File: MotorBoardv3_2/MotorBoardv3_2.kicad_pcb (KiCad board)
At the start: 2 copper layers, 128.3 x 158.1 mm, 98 parts, among them J1 Bump0, J11 GP2Y0A41SK0F, J12 GP2Y0A41SK0F, J13 GP2Y0A41SK0F, J15 7.2, J16 LP5.0, J17 ELA, J18 ERA, J19 Voltage Display, J2 Bump1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

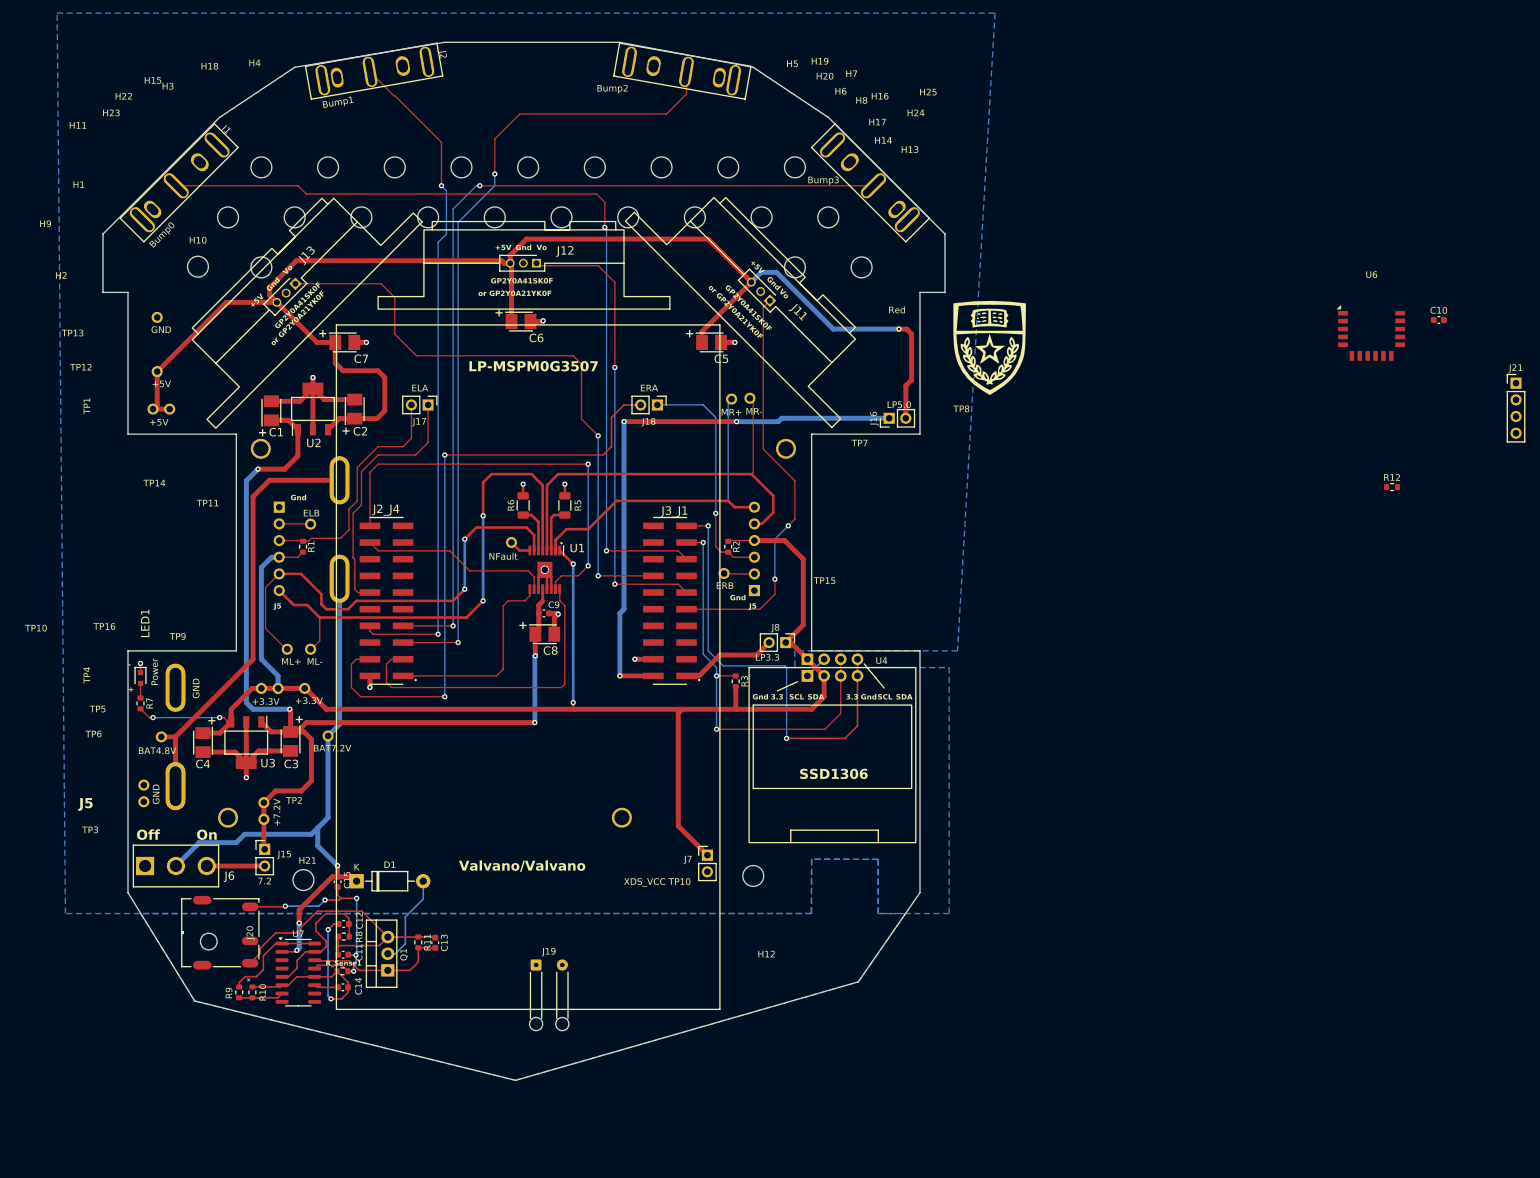
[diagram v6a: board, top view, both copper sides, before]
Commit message: routed RN4871 eval board pins
Also changed the positions of some silkscreen labels
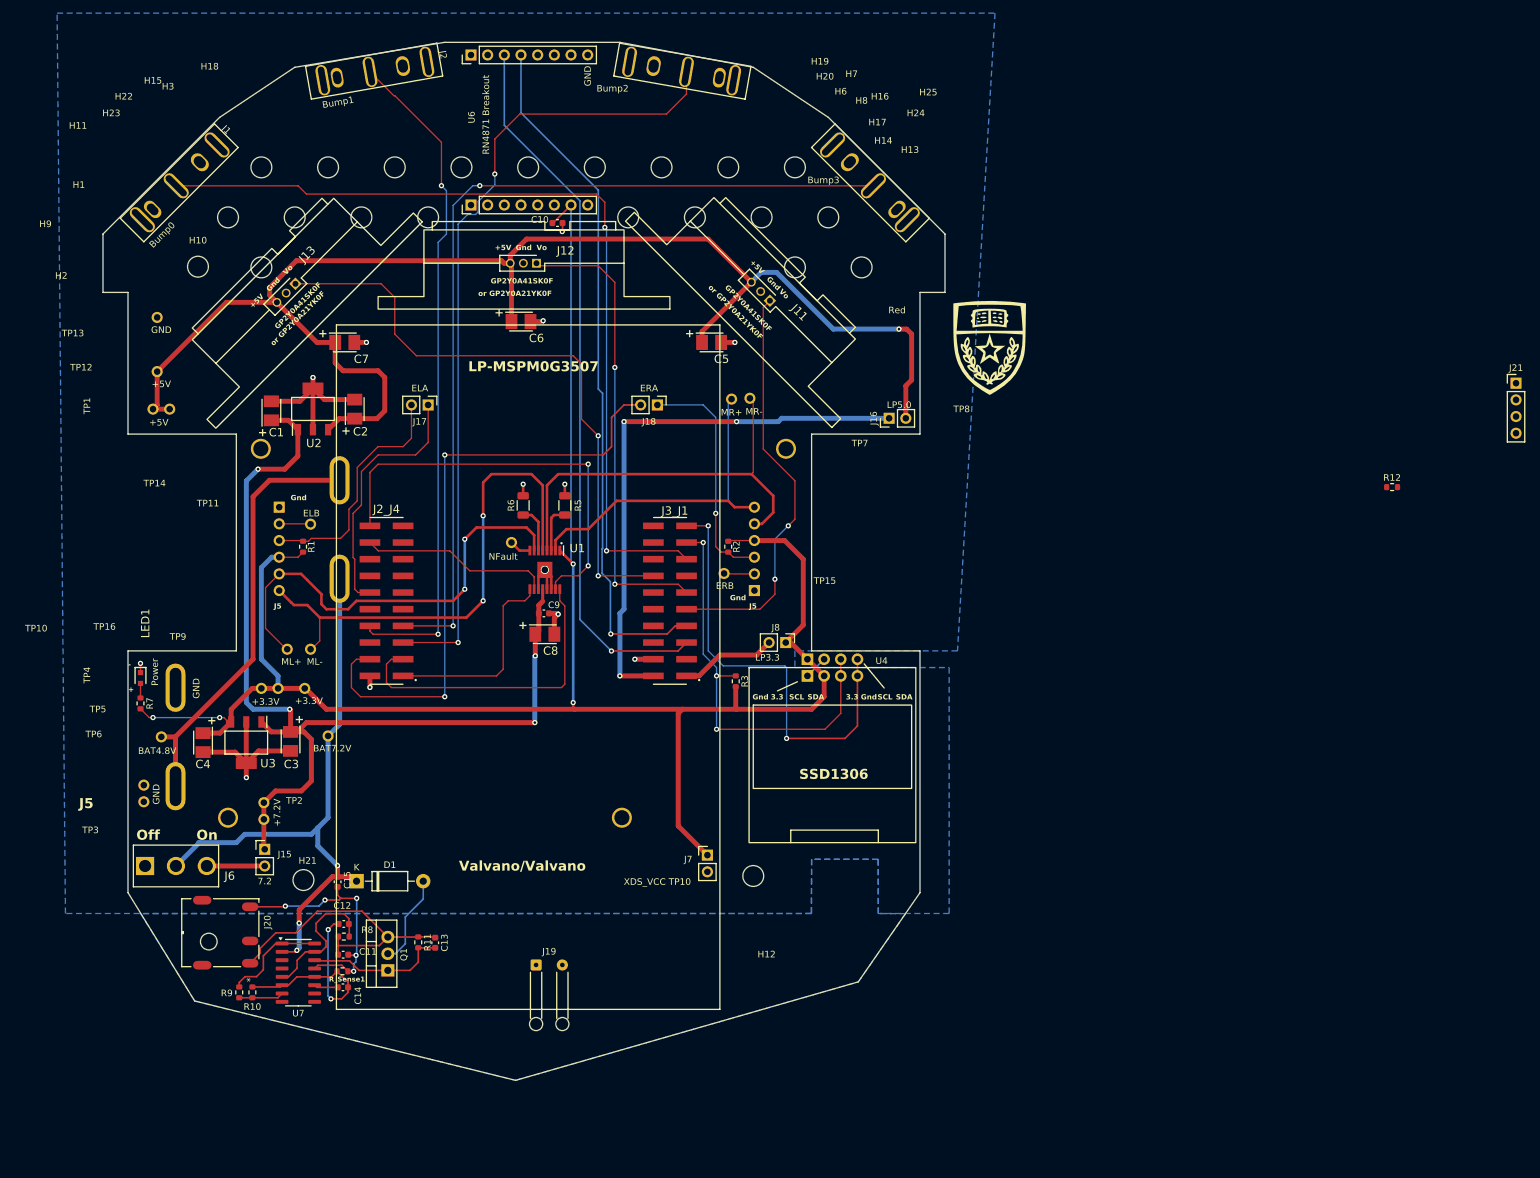
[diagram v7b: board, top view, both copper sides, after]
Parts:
- removed H4, H5: ~, RSLK2:MountingHole_4_40
- U6: footprint RF_Module:Microchip_RN4871 -> VoltageDisplay:RN4871_eval
- moved C10 135.1 mm to (113.7, 51.7)
- moved U6 119.0 mm to (120.1, 50.9), turned to 90 degrees
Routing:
- net PA9: track 0.00 -> 110.8 mm, vias 0 -> 1
- net PA8: track 0.00 -> 106.0 mm, vias 0 -> 1
- net +3V3: track 233.3 -> 292.1 mm
- net GND: track 113.5 -> 114.9 mm, vias 14 -> 15
- net PA28: track 122.8 -> 123.5 mm
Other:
- board text added: "RN4871 Breakout"

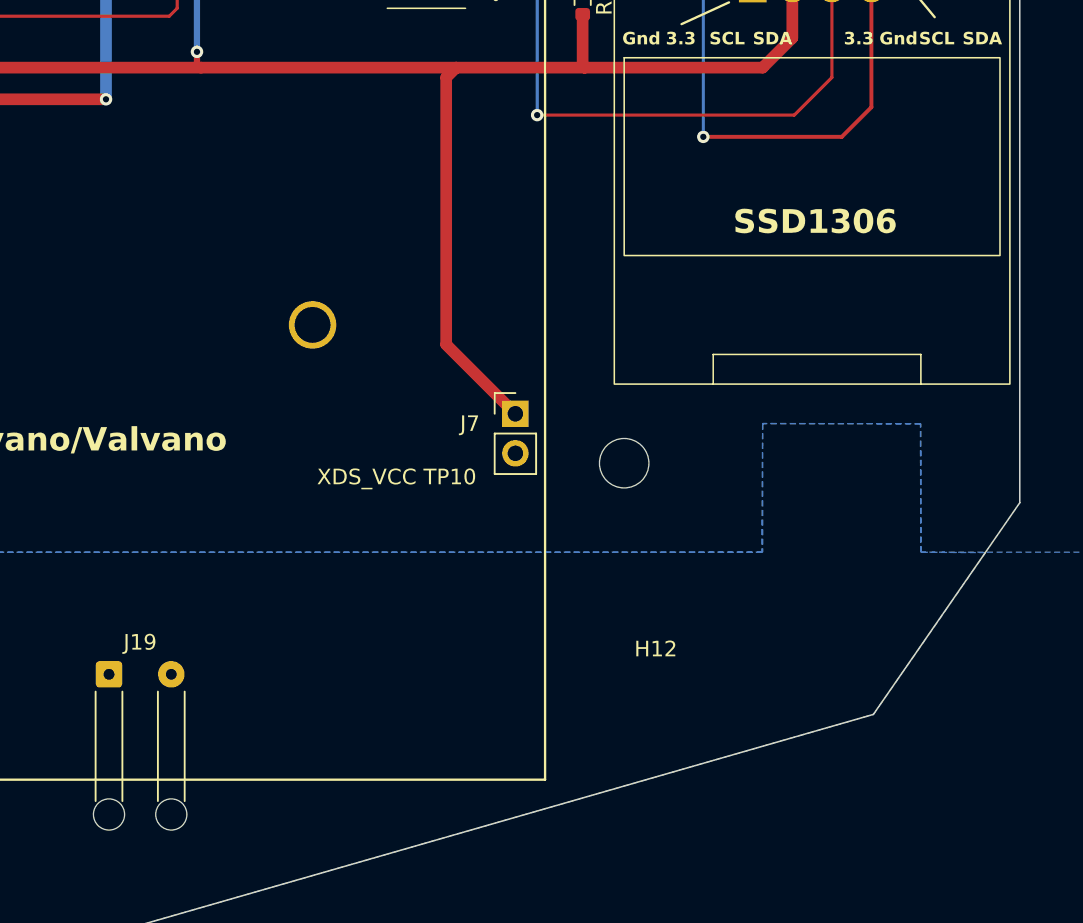
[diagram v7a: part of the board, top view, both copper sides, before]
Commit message: Added voltage display
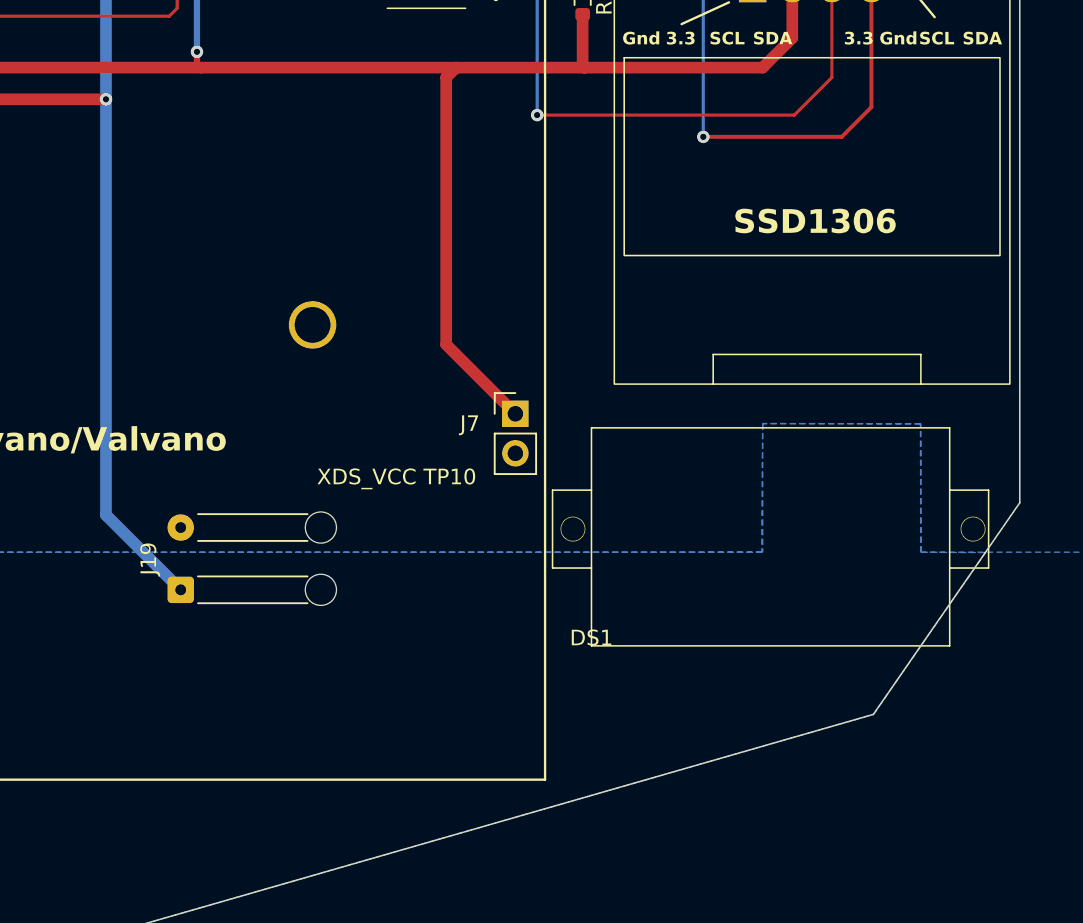
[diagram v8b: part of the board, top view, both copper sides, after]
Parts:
- removed H12: ~, RSLK2:MountingHole_4_40
- added DS1: ~, VoltageDisplay:PRT-14313, F.Cu at (141.4, 162.9)
- J19: value Voltage Display -> Voltage Display Port
- moved J19 7.12 mm to (115.0, 159.3), turned to 90 degrees
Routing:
- net +7.2V: track 151.8 -> 185.3 mm
